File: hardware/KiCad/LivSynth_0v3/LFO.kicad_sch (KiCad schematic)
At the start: 18 parts, among them Q1 2N3904, Q16 2N3904, Q17 2N3904, U6 TL074

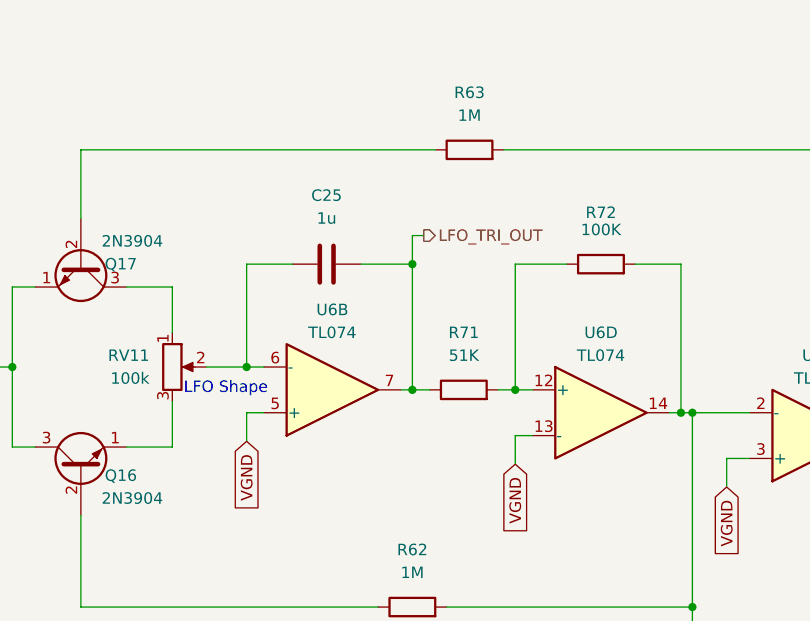
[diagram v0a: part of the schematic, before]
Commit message: Add another LFO cap for easier modding please MCU connectors to the backside Relocate reset button KiCad 7.0.1
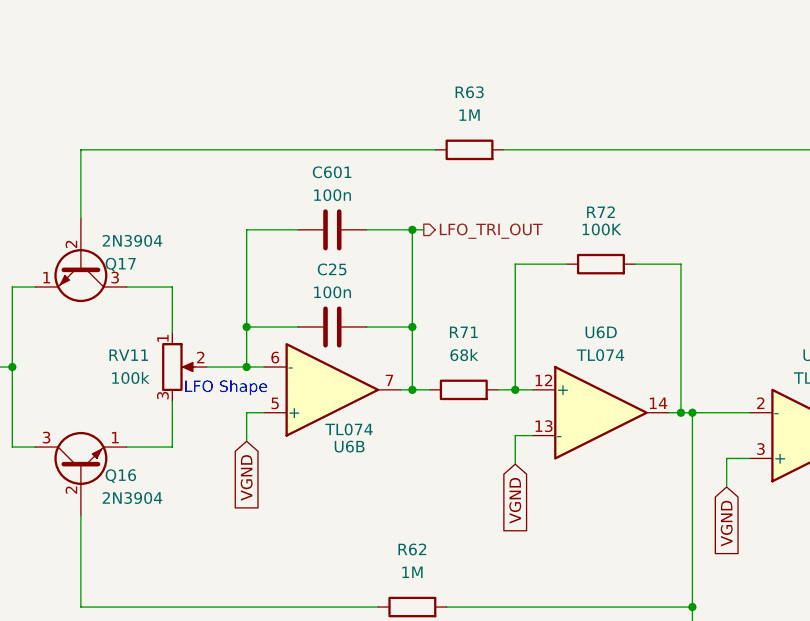
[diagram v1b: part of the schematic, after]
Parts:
- added C601: 100n, Capacitor_THT:C_Rect_L7.2mm_W2.5mm_P5.00mm_FKS2_FKP2_MKS2_MKP2, symbol Device:C
- C25: value 1u -> 100n; footprint Capacitor_THT:C_Rect_L7.2mm_W5.5mm_P5.00mm_FKS2_FKP2_MKS2_MKP2 -> Capacitor_THT:C_Rect_L7.2mm_W2.5mm_P5.00mm_FKS2_FKP2_MKS2_MKP2
- R71: value 51K -> 68k
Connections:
- net LFO_TRI_OUT: now also C601.2
- net at C25.1, RV11.2, U6.6 (-): now also C601.1
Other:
- moved on the sheet: C25

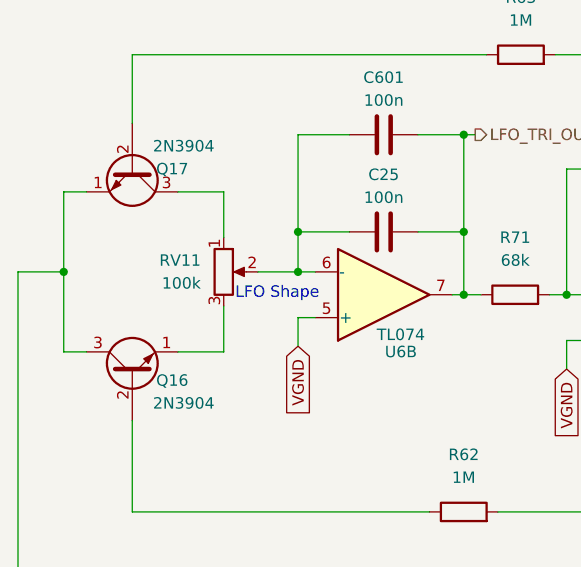
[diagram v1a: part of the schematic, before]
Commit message: RV11 = 100K update BOM RV2 = 100K C13 = 10n R23 = 470K
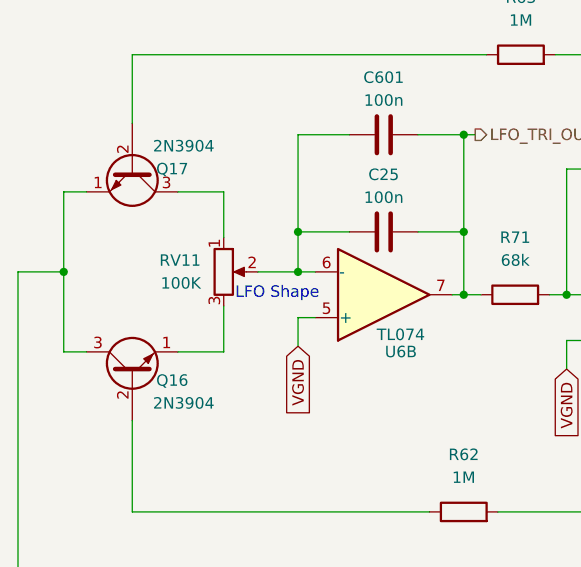
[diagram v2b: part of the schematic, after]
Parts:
- RV11: value 100k -> 100K
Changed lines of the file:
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@@
       (effects (font (size 1.27 1.27)) (justify right))
     )
-    (property "Value" "100k" (at 104.775 74.9299 0)
+    (property "Value" "100K" (at 104.775 74.9299 0)
       (effects (font (size 1.27 1.27)) (justify right))
     )
